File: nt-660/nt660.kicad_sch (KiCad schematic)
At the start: 156 parts, among them J1 USB_mini_micro_B, J2 ISP, K1 KEYSW, K10 KEYSW, K11 KEYSW, K12 KEYSW, K13 KEYSW, K14 KEYSW, K15 KEYSW, K16 KEYSW, K17 KEYSW, K18 KEYSW, K19 KEYSW, K2 KEYSW, K20 KEYSW, K21 KEYSW, K22 KEYSW, K23 KEYSW, K24 KEYSW, K25 KEYSW, K26 KEYSW, K27 KEYSW, K28 KEYSW, K29 KEYSW, K3 KEYSW, K30 KEYSW, K31 KEYSW, K32 KEYSW, K33 KEYSW, K34 KEYSW, K35 KEYSW, K36 KEYSW, K37 KEYSW, K38 KEYSW, K39 KEYSW, K4 KEYSW, K40 KEYSW, K41 KEYSW, K42 KEYSW, K43 KEYSW, K44 KEYSW, K44-1 KEYSW, K46 KEYSW, K46-1 KEYSW, K47 KEYSW, K48 KEYSW, K49 KEYSW, K5 KEYSW, K50 KEYSW, K51 KEYSW, K52 KEYSW, K53 KEYSW, K54 KEYSW, K55 KEYSW, K56 KEYSW, K57 KEYSW, K58 KEYSW, K59 KEYSW, K6 KEYSW, K61 KEYSW, K62 KEYSW, K63 KEYSW, K67 KEYSW, K7 KEYSW, K70 KEYSW, K71 KEYSW, K72 KEYSW, K73 KEYSW, K74 KEYSW, K75 KEYSW, K8 KEYSW, K9 KEYSW, SW1 Reset, U1 ATmega32U4, U2 USBLC6-2SC6, X1 CSTNE16M0V530000R0

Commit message: nt-660 rev1.1
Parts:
- added K62-1, K63-1: KEYSW, Keeb_switches:CHERRY_PLATE_125H, symbol keyboard_parts:KEYSW
- added K67-1: KEYSW, Keeb_switches:CHERRY_PCB_600C_H_F, symbol keyboard_parts:KEYSW
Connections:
- net col1: now also K62-1.2
- net col2: now also K63-1.2
- net col6: now also K67-1.2
- net at D63.2 (A), K63.1: now also K63-1.1
- net at D62.2 (A), K62.1: now also K62-1.1
- net at D67.2 (A), K67.1: now also K67-1.1
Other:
- moved on the sheet: D61, D62, D63, D67, D70, D71, D72, D73, D74, D75, K61, K62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

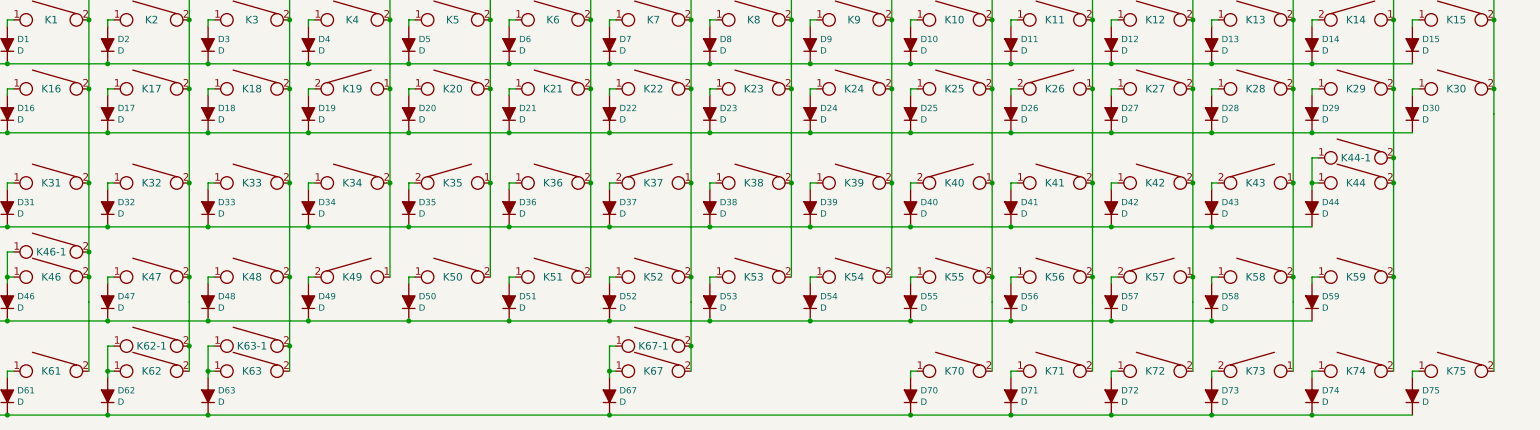
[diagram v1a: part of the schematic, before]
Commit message: Update PCB footprints/gerbers
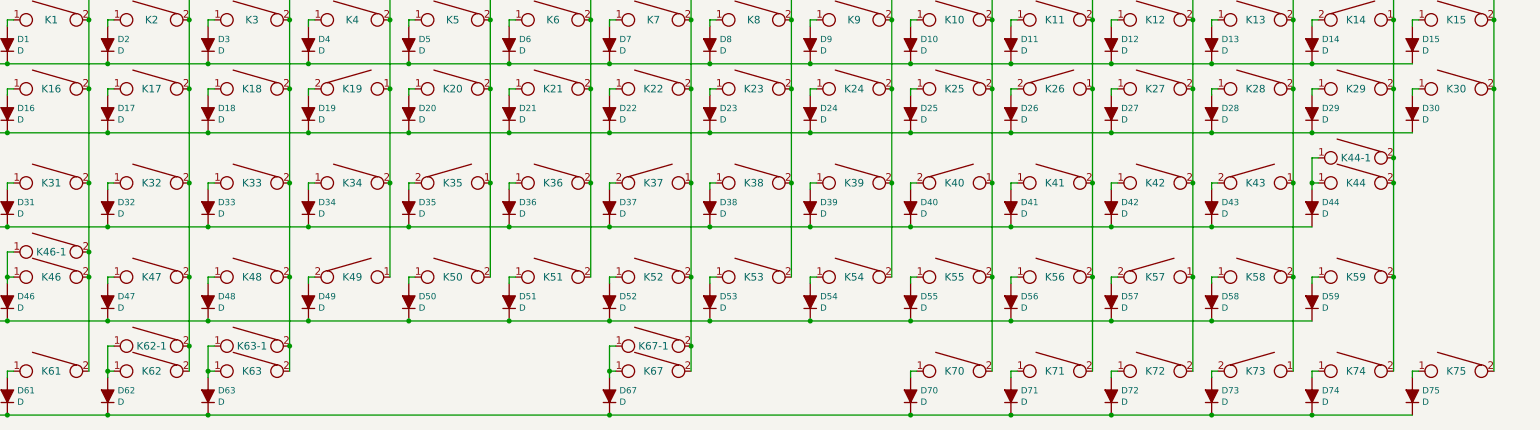
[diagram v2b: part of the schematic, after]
